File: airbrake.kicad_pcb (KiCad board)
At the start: 2 copper layers, 53.2 x 52.2 mm, 74 parts, among them IC1 SN74HCT125DR, J1 Molex Microfit, J2 Molex Microfit, J3 Molex Microfit, J4 Molex Microfit, J5 Molex Microfit, J6 Conn_02x03_Counter_Clockwise, U1 MS5607-02BA, U2 MMC5983MA, U3 STM32G431RBTx, U4 TMP275AIDGKR VSSOP8, U5 LP5912Q3.3DRVRQ1, U6 BMI088, U7 TPS62153, U8 USBLC6-2SC6, U9 W25Q256JVEIQTR, X1 1XXD32000MBA

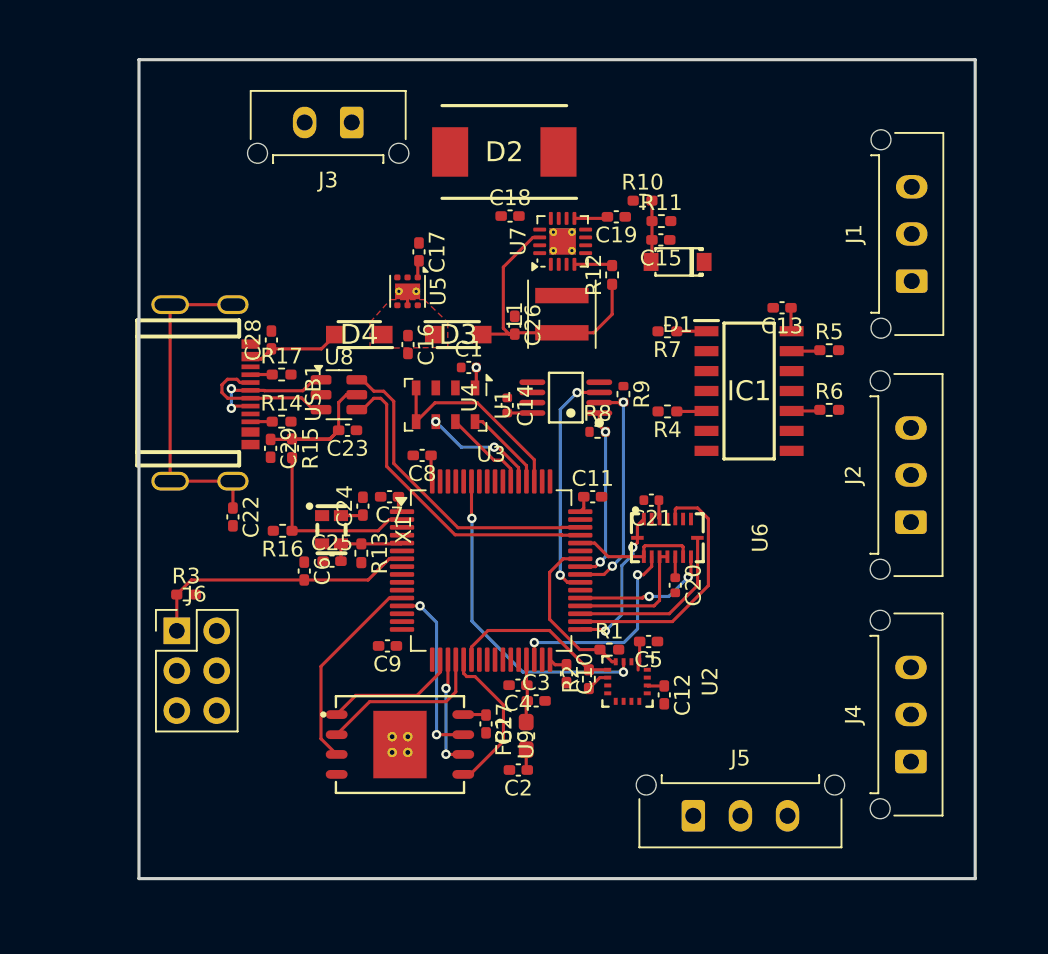
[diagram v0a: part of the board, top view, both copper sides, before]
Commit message: feat(pcb): trace routing
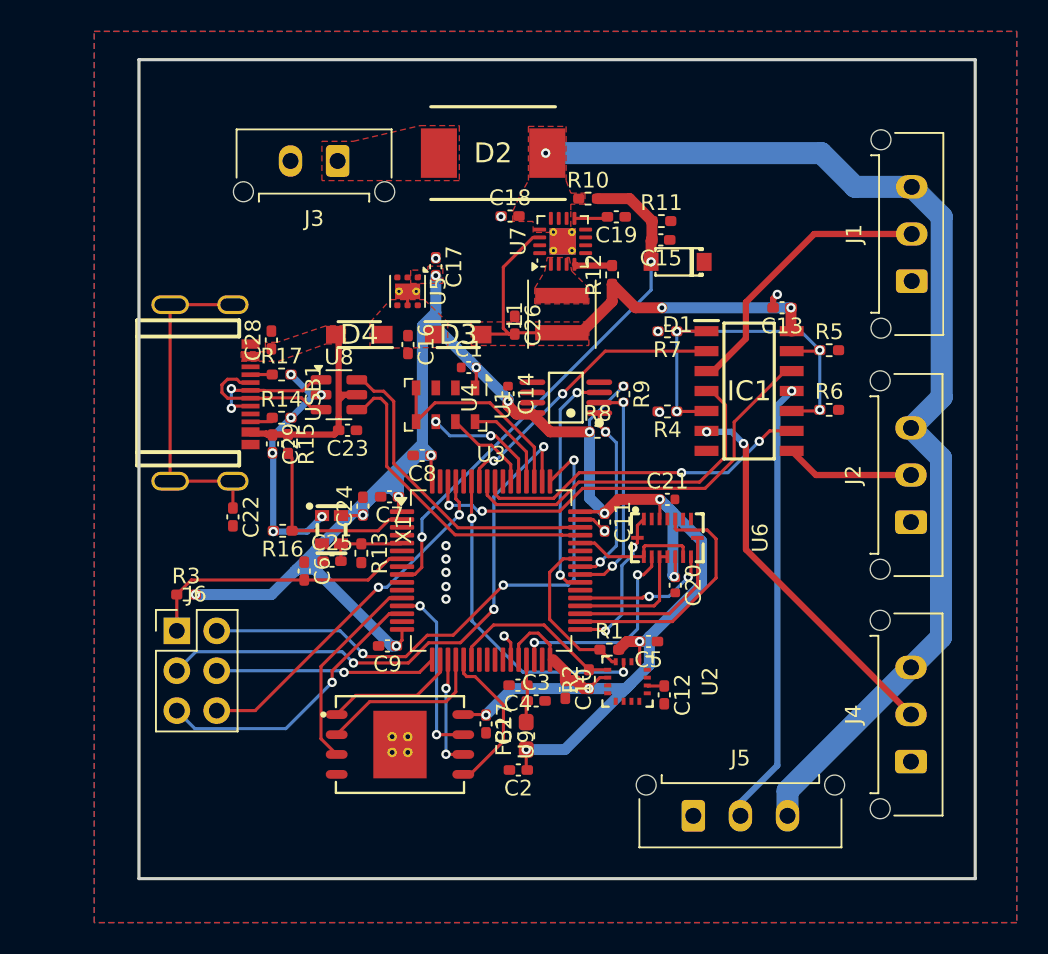
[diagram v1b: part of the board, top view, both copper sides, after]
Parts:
- moved R10 3.47 mm to (134.7, 42.9)
- moved J3 2.61 mm to (118.8, 40.5)
- moved C11 1.79 mm to (135.8, 63.5), turned to -90 degrees
- moved C17 1.43 mm to (125.0, 47.2)
- moved C21 1.02 mm to (139.8, 62.0), turned to 0 degrees
- moved C10 1.00 mm to (133.2, 74.2)
- moved C14 0.75 mm to (129.6, 55.3)
- moved D2 0.72 mm to (128.7, 40.0)
- moved R15 0.38 mm to (115.6, 58.5)
- moved C29 0.31 mm to (114.6, 58.5)
- moved R14 0.25 mm to (115.2, 56.9)
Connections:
- U3 pad 25: BAT_LEVEL -> unconnected-(U3-PB1-Pad25)
- U3 pad 9: unconnected-(U3-PC1-Pad9) -> BAT_LEVEL
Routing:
- net +3.3V: track 19.2 -> 161.7 mm, vias 1 -> 17
- net VBAT+: track 0.00 -> 70.7 mm, vias 0 -> 1
- net SWCLK: track 0.20 -> 36.3 mm, vias 0 -> 3
- net SWDIO: track 0.00 -> 35.2 mm, vias 0 -> 3
- net BAT_LEVEL: track 3.93 -> 33.6 mm, vias 0 -> 2
- net SERVO_D: track 0.00 -> 28.4 mm, vias 0 -> 1
- net PWM_D: track 0.00 -> 28.2 mm, vias 0 -> 2
- net SERVO_B: track 0.00 -> 24.3 mm, vias 0 -> 2
- net BOOT0: track 0.00 -> 22.8 mm, vias 0 -> 2
- net PWM_B: track 0.00 -> 22.1 mm
- net PWM_C: track 0.00 -> 21.6 mm, vias 0 -> 2
- net VBAT-: track 0.89 -> 21.5 mm, vias 0 -> 18
- net PWM_A: track 0.00 -> 18.4 mm, vias 0 -> 2
- net COMPANION_TX: track 0.00 -> 18.3 mm, vias 0 -> 1
- net /PWM_PD: track 7.43 -> 25.7 mm, vias 0 -> 4
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- added copper zone on F.Cu, net +3.3V
- added copper zone on F.Cu, net +5V
- added copper zone on F.Cu, net Net-(D2-A)
- added copper zone on F.Cu, net Net-(L1-Pad2)
- added copper zone on F.Cu, net VBAT+
- added copper zone on B.Cu, net VBAT-
- added copper zone on F.Cu, net VBAT-
- added copper zone on F.Cu, net VBUS

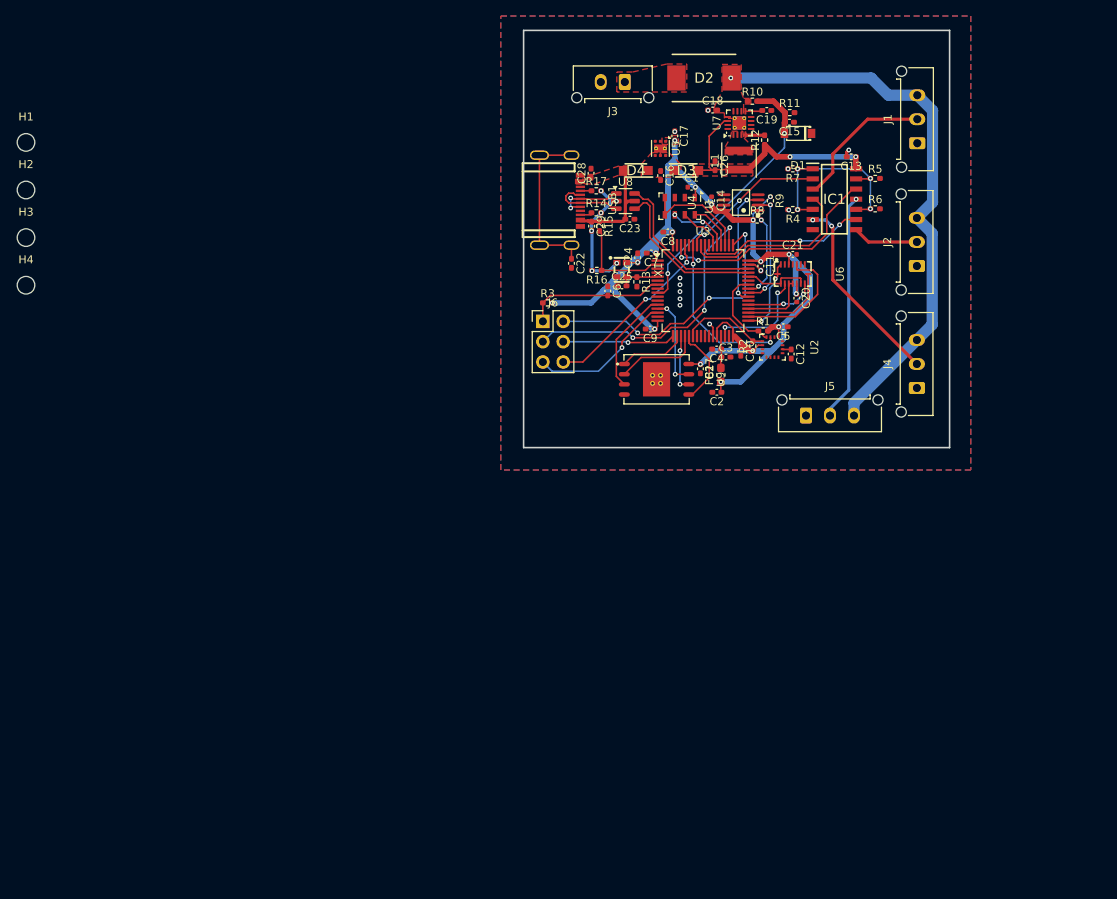
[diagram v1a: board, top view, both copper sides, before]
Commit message: feat(silscreen): adjust silkscreen and some trace
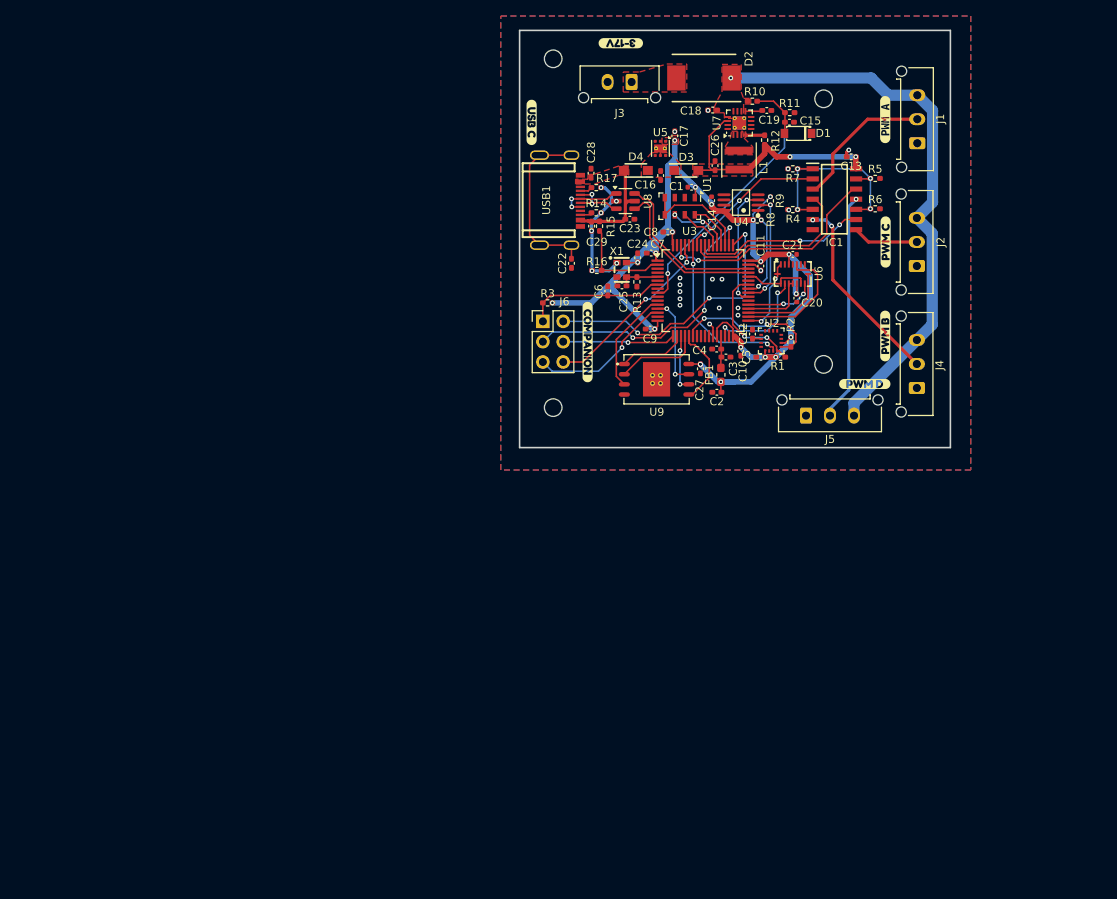
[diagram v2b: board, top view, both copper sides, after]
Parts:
- added kibuzzard-67AC9DAB: G***, kibuzzard-67AC9DAB, F.Cu at (151.3, 45.2)
- added kibuzzard-67AC9DCF: G***, kibuzzard-67AC9DCF, F.Cu at (151.3, 72.2)
- added kibuzzard-67AC9E05: G***, kibuzzard-67AC9E05, F.Cu at (151.3, 60.5)
- added kibuzzard-67AC9E3B: G***, kibuzzard-67AC9E3B, F.Cu at (148.8, 78.2)
- added kibuzzard-67AC9E4A: G***, kibuzzard-67AC9E4A, F.Cu at (107.1, 45.5)
- added kibuzzard-67AC9E5D: G***, kibuzzard-67AC9E5D, F.Cu at (118.2, 35.6)
- added kibuzzard-67AC9E80: G***, kibuzzard-67AC9E80, F.Cu at (114.1, 73.0)
- moved H2 100.3 mm to (143.6, 42.6)
- moved H4 100.2 mm to (143.6, 75.8)
- moved H3 69.2 mm to (109.8, 81.2)
- moved H1 66.7 mm to (109.8, 37.6)
- moved C12 5.44 mm to (134.7, 72.0), turned to 90 degrees
- moved R2 4.79 mm to (139.5, 73.0), turned to -90 degrees
- moved C5 4.72 mm to (135.8, 74.9), turned to 0 degrees
- moved R1 3.92 mm to (138.2, 74.9), turned to 180 degrees
- moved J3 0.85 mm to (119.6, 40.5)
- moved U2 0.81 mm to (137.1, 72.9), turned to 90 degrees
- moved R17 0.40 mm to (115.2, 53.7)
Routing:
- net MMC5983MA_SCL: track 11.2 -> 18.3 mm, vias 0 -> 2
- net MMC5983MA_SDA: track 10.6 -> 15.0 mm, vias 0 -> 2
- net D-: track 8.86 -> 7.39 mm, vias 0 -> 2
- net Net-(USB1-EH): track 21.0 -> 22.0 mm
- net VBAT-: track 21.5 -> 22.1 mm, vias 18 -> 23
- net D+: track 8.11 -> 7.51 mm
- net +3.3V: track 161.7 -> 161.8 mm, vias 17 -> 20
- net BAT_LEVEL: vias 2 -> 1
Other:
- board size 53.2 x 52.2 mm -> 53.8 x 52.2 mm

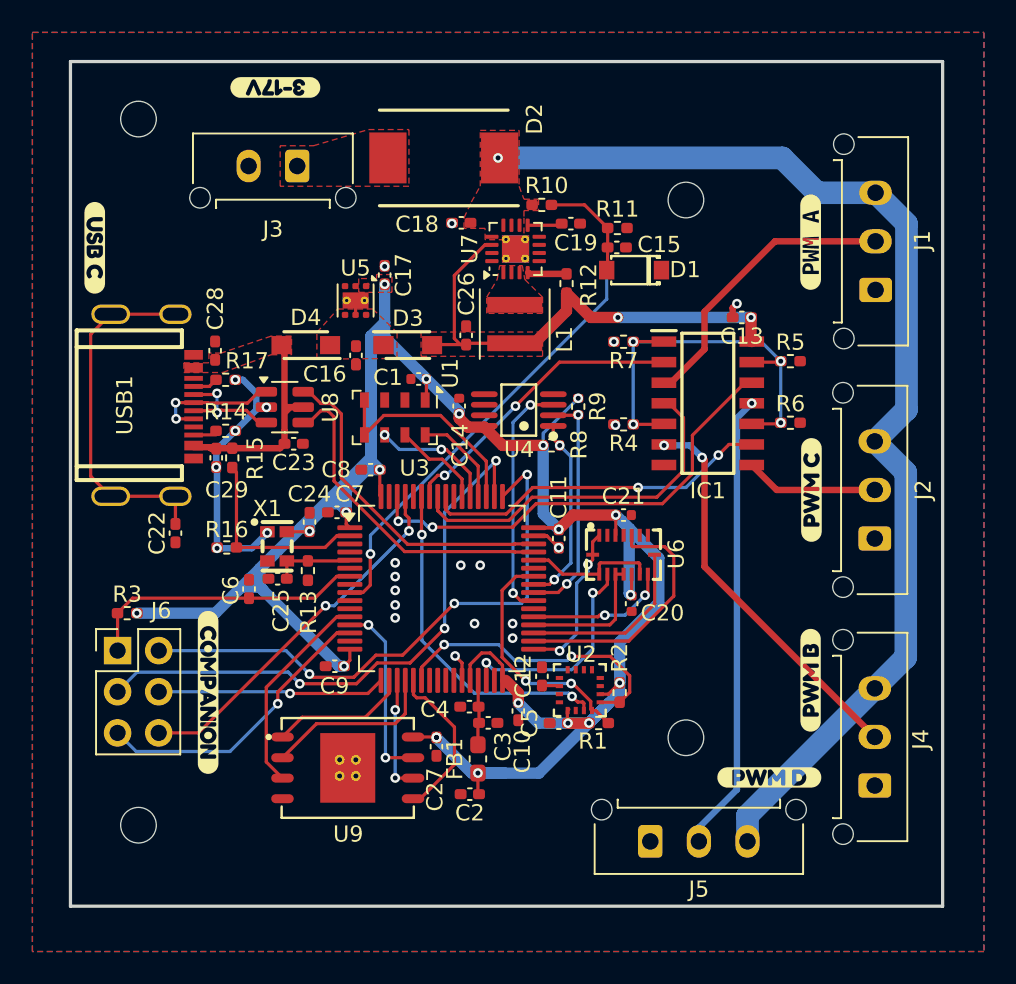
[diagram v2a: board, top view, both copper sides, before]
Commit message: feat(via): add stitching
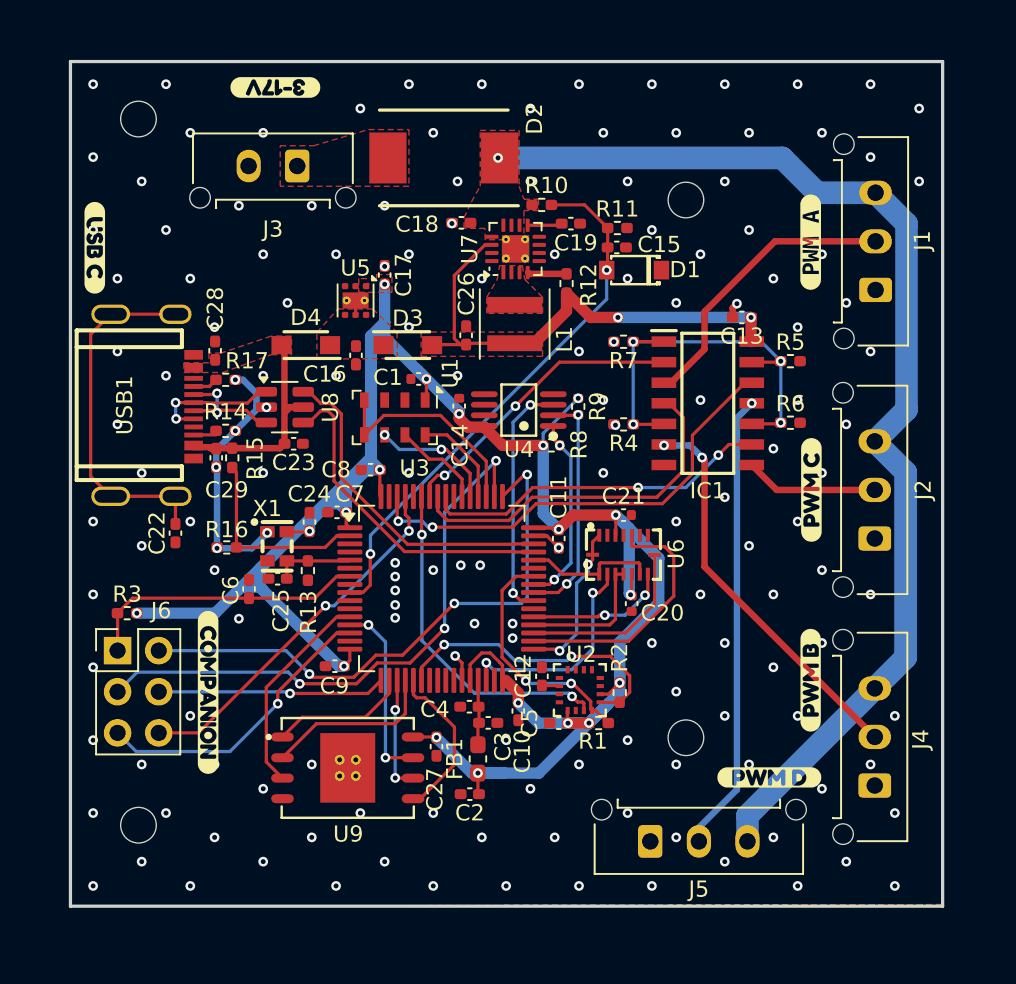
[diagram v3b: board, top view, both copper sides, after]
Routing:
- net VBAT-: track 22.1 -> 21.9 mm, vias 23 -> 158
- net +3.3V: track 161.8 -> 161.6 mm, vias 20 -> 19
- net BAT_LEVEL: vias 1 -> 2

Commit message: release: rev1
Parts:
- removed C22: 1nF, Capacitor_SMD:C_0402_1005Metric_Pad0.74x0.62mm_HandSolder
- removed C25: 10pF, Capacitor_SMD:C_0402_1005Metric_Pad0.74x0.62mm_HandSolder
- removed C28, C29: 10uF, Capacitor_SMD:C_0402_1005Metric_Pad0.74x0.62mm_HandSolder
- removed R17: 5.1k, Resistor_SMD:R_0402_1005Metric_Pad0.72x0.64mm_HandSolder
- removed kibuzzard-67AC9DAB: G***, kibuzzard-67AC9DAB
- added kibuzzard-67B37024: G***, kibuzzard-67B37024, F.Cu at (169.1, 89.3)
- C13, C16: footprint Capacitor_SMD:C_0402_1005Metric_Pad0.74x0.62mm_HandSolder -> Capacitor_SMD:C_1206_3216Metric_Pad1.33x1.80mm_HandSolder
- C24: value 100nF -> 10nF
- D1: footprint EasyEDA:SOD-123_L2.8-W1.8-LS3.7-RD -> SamacSys:SOD3716X135N
- D2: footprint Samacsys:DIOM7959X262N -> SamacSys:DIOM7959X262N
- D3, D4: footprint Samacsys:SODFL3616X98N -> SamacSys:SODFL3616X98N
- IC1: footprint Samacsys:SOIC127P600X175-14N -> SamacSys:SOIC127P600X175-14N
- L1: footprint Inductor_SMD:L_Coilcraft_XxL4020 -> SamacSys:XFL4020472MEC
- R13: value 100k -> 5.1k
- R14: value 5.1k -> 10k
- R15: value 10k -> 22k
- R16: value 22k -> 5.1k
- U1: value MS5607-02BA -> MS560702BA03-50
- U2: footprint EasyEDA:LGA-16_L3.0-W3.0-P0.50-BL_SQ -> SamacSys:MMC5983MA
- U4: value TMP275AIDGKR VSSOP8 -> TMP275AIDGKR; footprint EasyEDA:VSSOP-8_L3.0-W3.0-P0.65-LS5.0-BL -> SamacSys:SOP65P490X110-8N
- U9: footprint EasyEDA:WSON-8_L8.0-W6.10-P1.27-BL-EP -> SamacSys:SON127P800X600X80-9N-D
- USB1: value C169130 -> 10172013-00011LF; footprint EasyEDA:USB-C-SMD_TYPE-C3.1-02 -> SamacSys:1017201300011LF
- X1: value 1XXD32000MBA -> ECS-TXO-32CSMV-320-AN-TR; footprint EasyEDA:OSC-SMD_4P-L2.0-W1.6-BL_1XXD -> SamacSys:ECSTXO32CSMV320ANTR
- moved R2 53.3 mm to (157.7, 123.1), turned to 90 degrees
- moved R14 51.6 mm to (136.9, 103.7), turned to -90 degrees
- moved R15 51.3 mm to (136.3, 105.4), turned to 180 degrees
- moved C24 51.2 mm to (138.5, 110.3), turned to 180 degrees
- moved kibuzzard-67AC9E4A 51.0 mm to (128.7, 91.8), turned to 0 degrees
- moved R1 50.7 mm to (156.0, 122.4)
- moved U2 50.0 mm to (155.8, 119.2), turned to -90 degrees
- moved C26 49.9 mm to (147.4, 97.8), turned to 90 degrees
- moved H1 49.8 mm to (127.4, 84.2)
- moved X1 49.8 mm to (134.4, 111.1), turned to 0 degrees
- moved C12 49.7 mm to (152.6, 118.4)
- moved C10 49.5 mm to (151.3, 120.2)
- moved H4 49.5 mm to (162.6, 121.5)
- moved kibuzzard-67AC9E80 49.3 mm to (132.2, 118.9)
- moved C2 49.3 mm to (150.3, 124.3), turned to -90 degrees
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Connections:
- C24 pad 1: +3.3V -> HSE_IN
- C24 pad 2: VBAT- -> Net-(X1-OUTPUT)
- R13 pad 1: HSE_IN -> VBAT-
- R13 pad 2: VBAT- -> Net-(USB1-CC1)
- R14 pad 1: Net-(USB1-CC2) -> VBUS
- R14 pad 2: VBAT- -> BCD
- R15 pad 1: VBUS -> BCD
- R15 pad 2: BCD -> VBAT-
- R16 pad 1: BCD -> Net-(USB1-CC2)
- X1 pad 3: HSE_IN -> Net-(X1-OUTPUT)
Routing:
- net Net-(USB1-EH): track 22.0 -> 0.00 mm
- net VBAT-: track 21.9 -> 9.41 mm, vias 158 -> 22
- net BCD: track 12.0 -> 6.91 mm
- net BAT_LEVEL: track 33.6 -> 38.5 mm
- net +3.3V: track 161.6 -> 166.0 mm
- net +3.3VA: track 3.86 -> 7.29 mm
- net HSE_IN: track 4.94 -> 1.88 mm
- net MMC5983MA_SDA: track 15.0 -> 17.7 mm
- net Net-(X1-OUTPUT): track 0.00 -> 2.47 mm
- net VBUS: track 15.8 -> 17.6 mm, vias 0 -> 2
- net +5V: track 30.3 -> 32.1 mm
- net D+: track 7.51 -> 6.02 mm, vias 2 -> 0
- net BMI088_GYRO_CS: track 15.8 -> 16.9 mm
- net MMC5983MA_INT: track 21.0 -> 22.0 mm
- net W25Q_HOLD: track 11.5 -> 10.4 mm
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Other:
- board size 53.8 x 52.2 mm -> 53.9 x 52.1 mm
